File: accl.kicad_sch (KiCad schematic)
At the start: 3 parts, among them U6 ADXL343

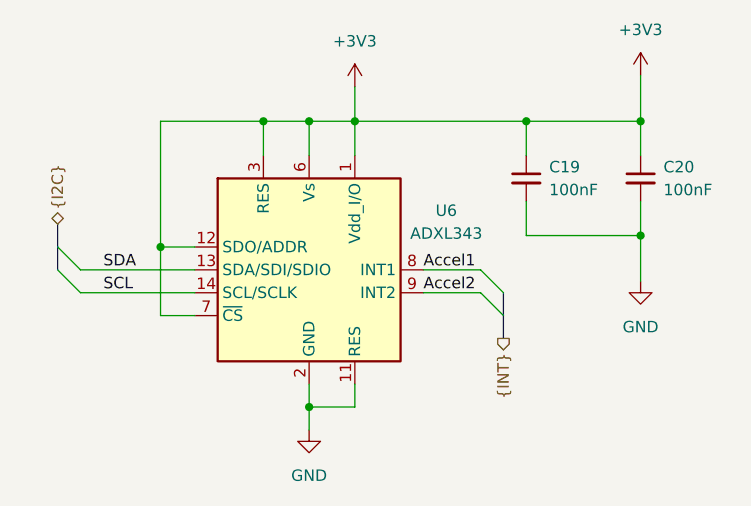
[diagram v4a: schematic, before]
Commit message: Changed placements of components
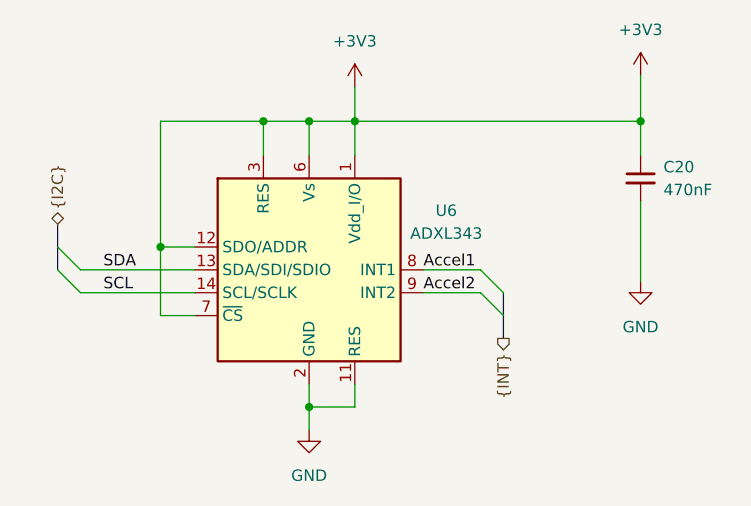
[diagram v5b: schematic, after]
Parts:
- removed C19: 100nF, Capacitor_SMD:C_0603_1608Metric, symbol Device:C_Small
- C20: value 100nF -> 470nF
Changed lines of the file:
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@@
   (junction (at 52.07 29.21) (diameter 0) (color 0 0 0 0)
   )
-  (junction (at 76.2 29.21) (diameter 0) (color 0 0 0 0)
-  )
   (junction (at 35.56 43.18) (diameter 0) (color 0 0 0 0)
   )
-  (junction (at 88.9 41.91) (diameter 0) (color 0 0 0 0)
-  )
   (junction (at 46.99 29.21) (diameter 0) (color 0 0 0 0)
   )
@@
     (stroke (width 0) (type default) (color 0 0 0 0))
   )
-  (wire (pts (xy 88.9 41.91) (xy 76.2 41.91))
-    (stroke (width 0) (type default) (color 0 0 0 0))
-  )
-  (wire (pts (xy 76.2 29.21) (xy 76.2 33.02))
-    (stroke (width 0) (type default) (color 0 0 0 0))
-  )
   (wire (pts (xy 52.07 58.42) (xy 52.07 60.96))
     (stroke (width 0) (type default) (color 0 0 0 0))
   )
-  (wire (pts (xy 76.2 38.1) (xy 76.2 41.91))
-    (stroke (width 0) (type default) (color 0 0 0 0))
-  )
   (wire (pts (xy 52.07 33.02) (xy 52.07 29.21))
     (stroke (width 0) (type default) (color 0 0 0 0))
@@
     (stroke (width 0) (type default) (color 0 0 0 0))
   )
-  (wire (pts (xy 76.2 29.21) (xy 88.9 29.21))
-    (stroke (width 0) (type default) (color 0 0 0 0))
-  )
-  (wire (pts (xy 88.9 38.1) (xy 88.9 41.91))
+  (wire (pts (xy 57.15 29.21) (xy 88.9 29.21))
+    (stroke (width 0) (type default) (color 0 0 0 0))
+  )
+  (wire (pts (xy 88.9 38.1) (xy 88.9 46.99))
     (stroke (width 0) (type default) (color 0 0 0 0))
   )
@@
     (stroke (width 0) (type default) (color 0 0 0 0))
   )
-  (wire (pts (xy 88.9 41.91) (xy 88.9 46.99))
-    (stroke (width 0) (type default) (color 0 0 0 0))
-  )
   (wire (pts (xy 57.15 29.21) (xy 57.15 33.02))
-    (stroke (width 0) (type default) (color 0 0 0 0))
-  )
-  (wire (pts (xy 57.15 29.21) (xy 76.2 29.21))
     (stroke (width 0) (type default) (color 0 0 0 0))
   )
@@
       (effects (font (size 1.27 1.27)) (justify left))
     )
-    (property "Value" "100nF" (id 1) (at 91.44 36.8362 0)
+    (property "Value" "470nF" (id 1) (at 91.44 36.8362 0)
       (effects (font (size 1.27 1.27)) (justify left))
     )
@@
     (pin "1")
   )
-  (symbol (lib_id "Device:C_Small") (at 76.2 35.56 0) (unit 1)
-    (in_bom yes) (on_board yes) (fields_autoplaced)
-    (property "Reference" "C19" (id 0) (at 78.74 34.2962 0)
-      (effects (font (size 1.27 1.27)) (justify left))
-    )
-    (property "Value" "100nF" (id 1) (at 78.74 36.8362 0)
-      (effects (font (size 1.27 1.27)) (justify left))
-    )
-    (property "Footprint" "Capacitor_SMD:C_0603_1608Metric" (id 2) (at 76.2 35.56 0)
-      (effects (font (size 1.27 1.27)) hide)
-    )
-    (property "Datasheet" "~" (id 3) (at 76.2 35.56 0)
-      (effects (font (size 1.27 1.27)) hide)
-    )
-    (pin "1")
-    (pin "2")
-  )
 )

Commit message: Added polyfuse
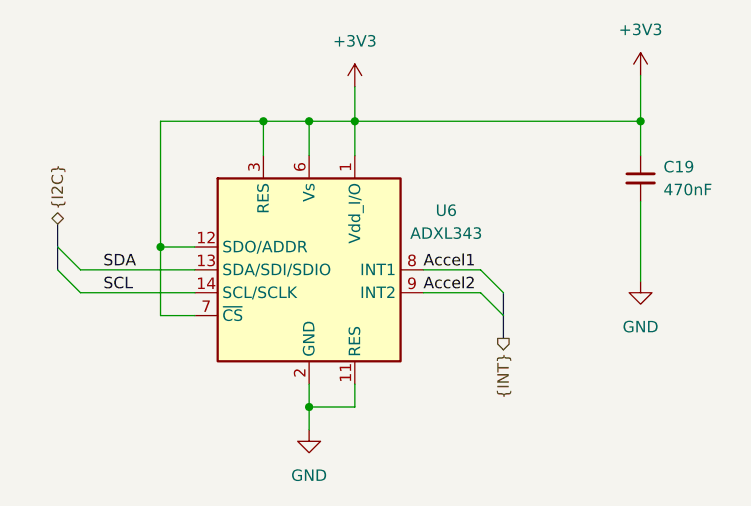
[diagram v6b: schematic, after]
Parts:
- renumbered C20 to C19
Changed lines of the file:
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@@
   (symbol (lib_id "power:+3V3") (at 57.15 25.4 0) (unit 1)
     (in_bom yes) (on_board yes) (fields_autoplaced)
-    (property "Reference" "#PWR037" (id 0) (at 57.15 29.21 0)
+    (property "Reference" "#PWR035" (id 0) (at 57.15 29.21 0)
       (effects (font (size 1.27 1.27)) hide)
     )
@@
   (symbol (lib_id "Device:C_Small") (at 88.9 35.56 0) (unit 1)
     (in_bom yes) (on_board yes) (fields_autoplaced)
-    (property "Reference" "C20" (id 0) (at 91.44 34.2962 0)
+    (property "Reference" "C19" (id 0) (at 91.44 34.2962 0)
       (effects (font (size 1.27 1.27)) (justify left))
     )
@@
   (symbol (lib_id "power:GND") (at 52.07 63.5 0) (unit 1)
     (in_bom yes) (on_board yes) (fields_autoplaced)
-    (property "Reference" "#PWR036" (id 0) (at 52.07 69.85 0)
+    (property "Reference" "#PWR034" (id 0) (at 52.07 69.85 0)
       (effects (font (size 1.27 1.27)) hide)
     )
@@
   (symbol (lib_id "power:+3V3") (at 88.9 24.13 0) (unit 1)
     (in_bom yes) (on_board yes) (fields_autoplaced)
-    (property "Reference" "#PWR038" (id 0) (at 88.9 27.94 0)
+    (property "Reference" "#PWR036" (id 0) (at 88.9 27.94 0)
       (effects (font (size 1.27 1.27)) hide)
     )
@@
   (symbol (lib_id "power:GND") (at 88.9 46.99 0) (unit 1)
     (in_bom yes) (on_board yes) (fields_autoplaced)
-    (property "Reference" "#PWR039" (id 0) (at 88.9 53.34 0)
+    (property "Reference" "#PWR037" (id 0) (at 88.9 53.34 0)
       (effects (font (size 1.27 1.27)) hide)
     )

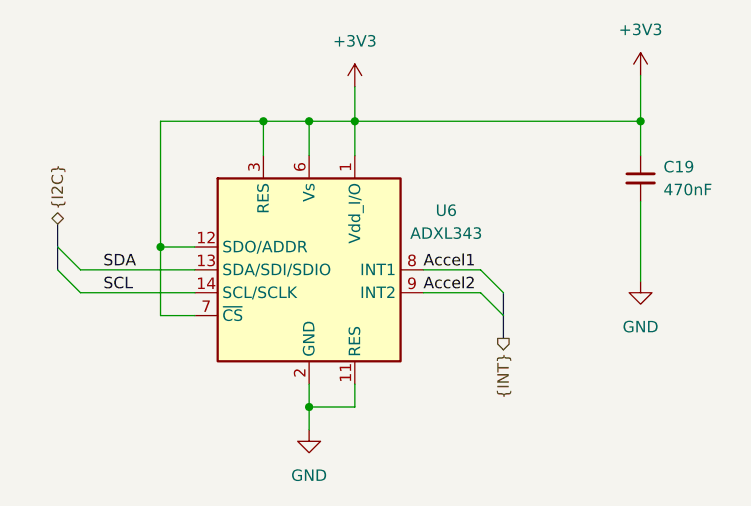
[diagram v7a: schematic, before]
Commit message: Geographical reannotated
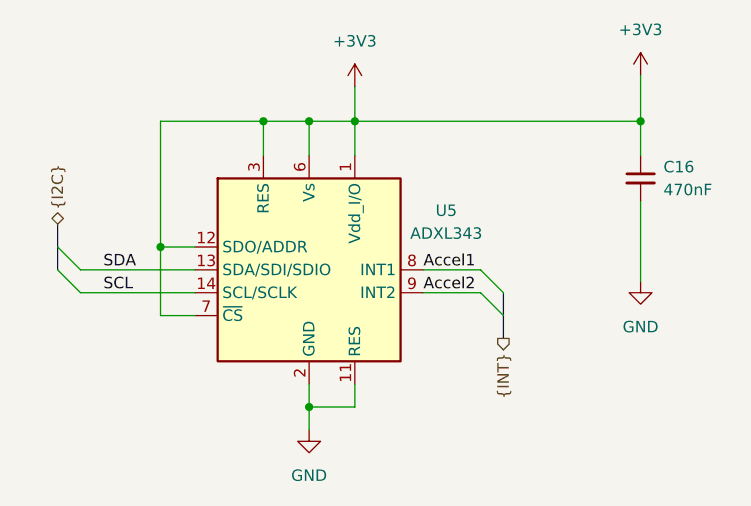
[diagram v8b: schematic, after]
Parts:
- renumbered C19 to C16, U6 to U5
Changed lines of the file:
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@@
   (symbol (lib_id "Sensor_Motion:ADXL343") (at 52.07 45.72 0) (unit 1)
     (in_bom yes) (on_board yes) (fields_autoplaced)
-    (property "Reference" "U6" (id 0) (at 67.31 39.1412 0))
+    (property "Reference" "U5" (id 0) (at 67.31 39.1412 0))
     (property "Value" "ADXL343" (id 1) (at 67.31 41.6812 0))
     (property "Footprint" "Package_LGA:LGA-14_3x5mm_P0.8mm_LayoutBorder1x6y" (id 2) (at 52.07 45.72 0)
@@
   (symbol (lib_id "Device:C_Small") (at 88.9 35.56 0) (unit 1)
     (in_bom yes) (on_board yes) (fields_autoplaced)
-    (property "Reference" "C19" (id 0) (at 91.44 34.2962 0)
+    (property "Reference" "C16" (id 0) (at 91.44 34.2962 0)
       (effects (font (size 1.27 1.27)) (justify left))
     )
